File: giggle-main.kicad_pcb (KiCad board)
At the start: 2 copper layers, 97.5 x 97 mm, 27 parts, among them J1 CONN_05X2SHD, J2 CONN_05X2SHD

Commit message: finished main side.
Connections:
- Promicro pad B1: (no net) -> N-col-0
- Promicro pad B2: (no net) -> N-row-1
- Promicro pad B3: (no net) -> N-col-4
- Promicro pad B4: (no net) -> N-row-2
- Promicro pad B5: (no net) -> N-row-3
- Promicro pad B6: (no net) -> N-row-0
- Promicro pad C6: (no net) -> N-col-8
- Promicro pad D0: (no net) -> N-col-11
- Promicro pad D1: (no net) -> N-col-10
- Promicro pad D4: (no net) -> N-col-12
- Promicro pad D7: (no net) -> N-col-7
- Promicro pad E6: (no net) -> N-col-6
- Promicro pad F4: (no net) -> N-col-5
- Promicro pad F5: (no net) -> N-col-3
- Promicro pad F6: (no net) -> N-col-2
- Promicro pad F7: (no net) -> N-col-1
- Promicro pad RX1: (no net) -> N-col-9
- Promicro pad TX0: (no net) -> N-col-13
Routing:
- net N-col-13: track 0.00 -> 100.8 mm
- net N-col-9: track 0.00 -> 90.7 mm
- net N-col-5: track 43.2 -> 131.1 mm
- net N-col-10: track 0.00 -> 83.6 mm
- net N-col-11: track 0.00 -> 79.9 mm
- net N-col-12: track 0.00 -> 78.3 mm
- net N-col-3: track 0.00 -> 69.0 mm
- net N-col-6: track 43.2 -> 110.7 mm
- net N-row-2: track 250.9 -> 316.6 mm
- net N-col-2: track 0.00 -> 65.5 mm
- net N-row-3: track 259.0 -> 323.9 mm
- net N-col-1: track 0.00 -> 61.2 mm
- net N-col-0: track 0.00 -> 58.3 mm
- net N-row-1: track 205.3 -> 254.6 mm
- net N-col-4: track 0.00 -> 46.7 mm
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
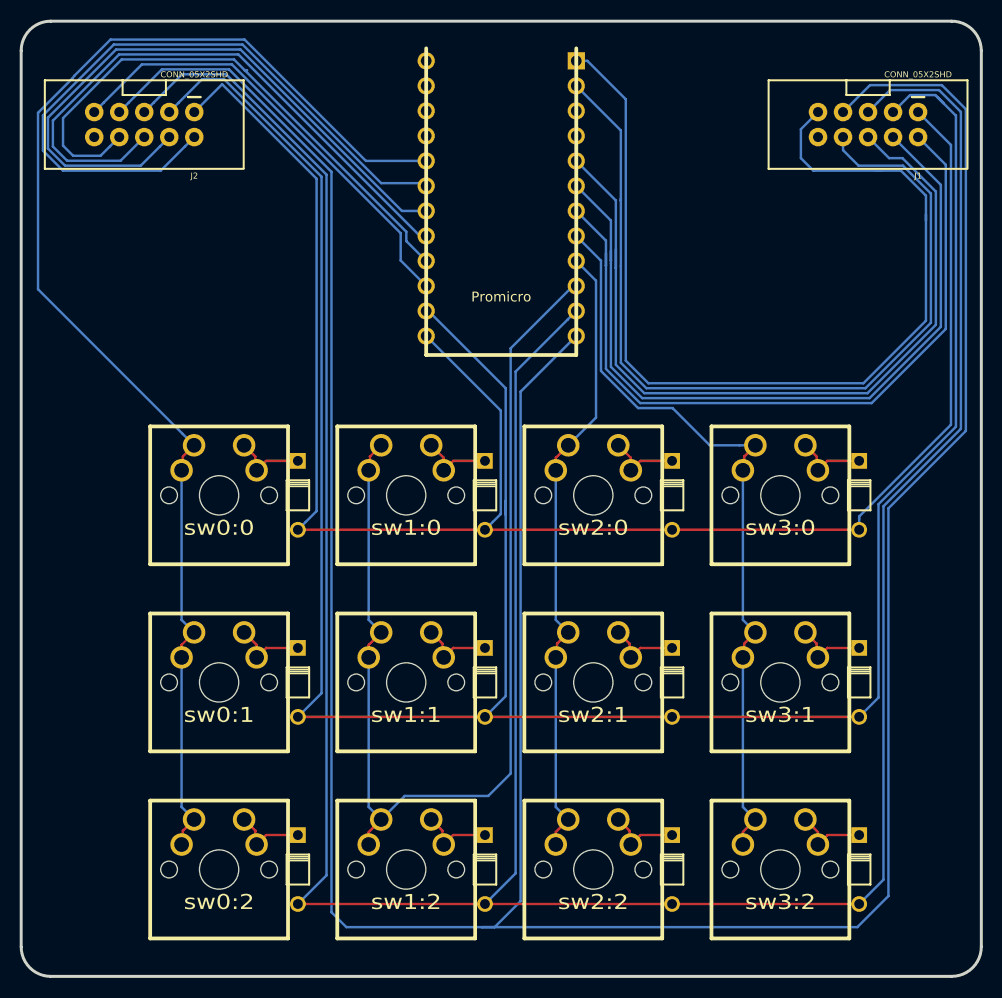
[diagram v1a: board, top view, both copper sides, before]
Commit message: some thing.
1. added another connector on side part.
2. nicer traces.
3. added the giggle text.
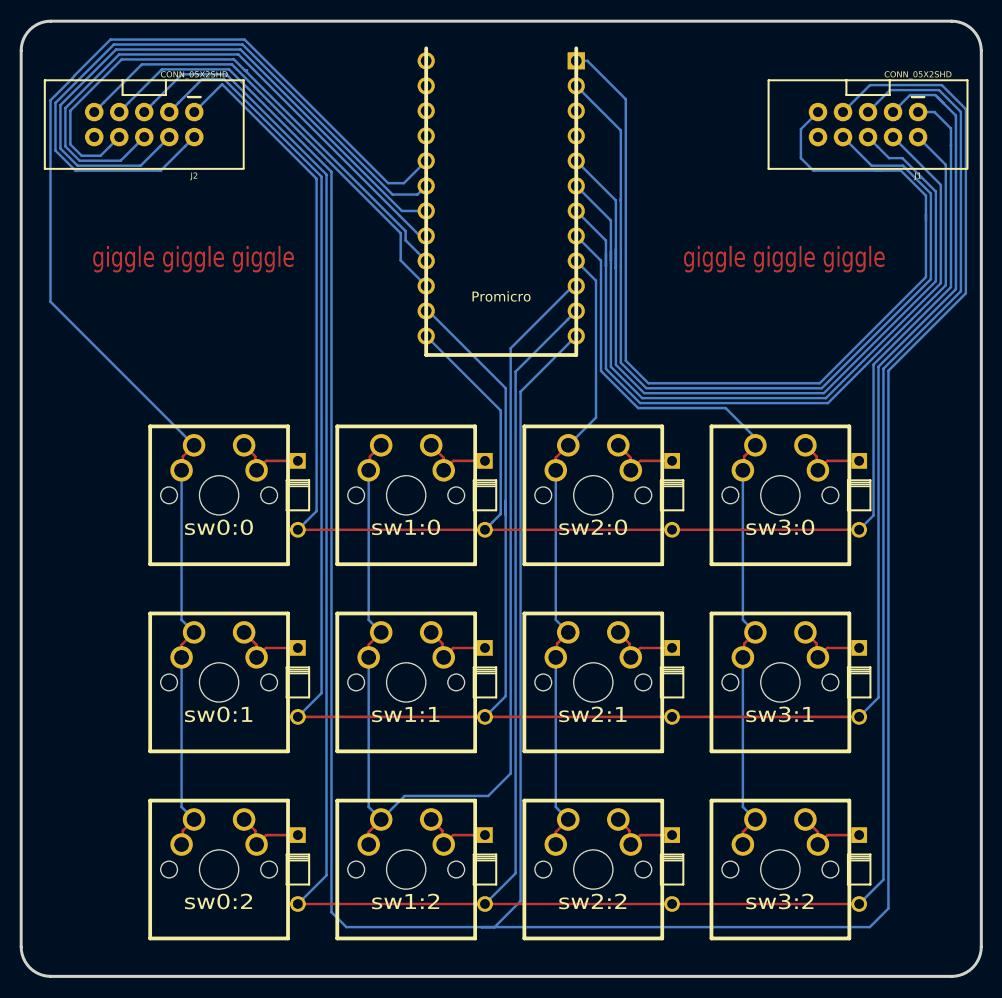
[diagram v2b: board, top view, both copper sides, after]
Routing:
- net N-col-9: track 90.7 -> 87.3 mm
- net N-col-12: track 78.3 -> 75.7 mm
- net N-col-11: track 79.9 -> 77.3 mm
- net N-col-10: track 83.6 -> 81.0 mm
- net N-col-13: track 100.8 -> 98.2 mm
- net N-col-2: track 65.5 -> 63.7 mm
- net N-col-1: track 61.2 -> 59.4 mm
- net N-col-0: track 58.3 -> 57.2 mm
- net N-col-3: track 69.0 -> 68.0 mm
- net N-row-0: track 182.1 -> 183.2 mm
- net N-col-5: track 131.1 -> 132.0 mm
- net N-row-3: track 323.9 -> 324.6 mm
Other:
- board text added: "giggle giggle giggle"

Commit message: 4x4 for main.
because why not?
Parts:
- added d0:3: , DIODE, F.Cu at (55.6, 114.2)
- added d1:3: , DIODE, F.Cu at (74.6, 114.2)
- added d2:3: , DIODE, F.Cu at (93.6, 114.2)
- added d3:3: , DIODE, F.Cu at (112.6, 114.2)
- added sw0:3: , MX_FLIP, F.Cu at (47.6, 114.2)
- added sw1:3: , MX_FLIP, F.Cu at (66.6, 114.2)
- added sw2:3: , MX_FLIP, F.Cu at (85.6, 114.2)
- added sw3:3: , MX_FLIP, F.Cu at (104.6, 114.2)
- moved d0:0 19.0 mm to (55.6, 57.1)
- moved d1:0 19.0 mm to (74.6, 57.1)
- moved d2:0 19.0 mm to (93.6, 57.1)
- moved d3:0 19.0 mm to (112.6, 57.1)
- moved sw0:0 19.0 mm to (47.6, 57.1)
- moved sw1:0 19.0 mm to (66.6, 57.1)
- moved sw2:0 19.0 mm to (85.6, 57.1)
- moved sw3:0 19.0 mm to (104.6, 57.1)
- moved d0:1 19.0 mm to (55.6, 76.2)
- moved d0:2 19.0 mm to (55.6, 95.2)
- moved d1:1 19.0 mm to (74.6, 76.2)
- moved d1:2 19.0 mm to (74.6, 95.2)
- moved d2:1 19.0 mm to (93.6, 76.2)
- moved d2:2 19.0 mm to (93.6, 95.2)
- moved d3:1 19.0 mm to (112.6, 76.2)
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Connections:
- Promicro pad B1: N-col-0 -> N-row-0
- Promicro pad B2: N-row-1 -> N-row-2
- Promicro pad B3: N-col-4 -> N-row-1
- Promicro pad B4: N-row-2 -> N-col-9
- Promicro pad B5: N-row-3 -> N-col-13
- Promicro pad B6: N-row-0 -> N-row-3
- Promicro pad C6: N-col-8 -> N-col-12
- Promicro pad D0: N-col-11 -> N-col-0
- Promicro pad D1: N-col-10 -> N-col-1
- Promicro pad D4: N-col-12 -> N-col-4
- Promicro pad D7: N-col-7 -> N-col-11
- Promicro pad E6: N-col-6 -> N-col-10
- Promicro pad F5: N-col-3 -> N-col-6
- Promicro pad F6: N-col-2 -> N-col-7
- Promicro pad F7: N-col-1 -> N-col-8
- Promicro pad RX1: N-col-9 -> N-col-2
- Promicro pad TX0: N-col-13 -> N-col-3
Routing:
- net N-row-2: track 316.6 -> 190.5 mm
- net N-row-3: track 324.6 -> 210.5 mm
- net N-row-1: track 254.6 -> 170.4 mm
- net N-col-13: track 98.2 -> 19.6 mm
- net N-col-9: track 87.3 -> 30.1 mm
- net N-col-10: track 81.0 -> 33.7 mm
- net N-col-11: track 77.3 -> 39.0 mm
- net N-col-4: track 46.7 -> 84.1 mm
- net N-row-0: track 183.2 -> 150.4 mm
- net N-col-12: track 75.7 -> 44.3 mm
- net N-col-3: track 68.0 -> 47.9 mm
- net N-col-5: track 132.0 -> 113.9 mm
- net N-col-7: track 63.9 -> 80.9 mm
- net N-col-0: track 57.2 -> 71.8 mm
- net N-col-6: track 110.7 -> 97.4 mm
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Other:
- board text added: "giggle giggle giggle giggle giggle giggle giggle giggle giggle giggle giggle giggle"
- board text removed: "giggle giggle giggle"

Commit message: looks better, i guess.
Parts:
- moved Promicro 6.00 mm to (85.0, 38.5)
- turned J1 to 270 degrees
- turned J2 to 270 degrees
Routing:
- net N-row-2: track 190.5 -> 233.1 mm
- net N-row-3: track 210.5 -> 251.1 mm
- net N-row-1: track 170.4 -> 207.2 mm
- net N-row-0: track 150.4 -> 185.6 mm
- net N-col-4: track 84.1 -> 54.0 mm
- net N-col-3: track 47.9 -> 63.6 mm
- net N-col-9: track 30.1 -> 20.9 mm
- net N-col-2: track 53.8 -> 62.0 mm
- net N-col-0: track 71.8 -> 63.7 mm
- net N-col-13: track 19.6 -> 12.1 mm
- net N-col-10: track 33.7 -> 26.4 mm
- net N-col-11: track 39.0 -> 31.9 mm
- net N-col-12: track 44.3 -> 37.3 mm
- net N-col-8: track 79.0 -> 85.0 mm
- net N-col-6: track 97.4 -> 91.4 mm
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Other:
- net class Default added: clearance 0.254, trace_width 0.25, via_dia 0.889, via_drill 0.635

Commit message: forgot the pcb. lmao.
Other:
- net class Default removed

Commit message: yes.
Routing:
- net N-col-5: track 107.9 -> 188.9 mm
- net N-col-6: track 91.4 -> 168.6 mm
- net N-col-7: track 76.5 -> 148.3 mm
- net N-col-8: track 85.0 -> 128.0 mm

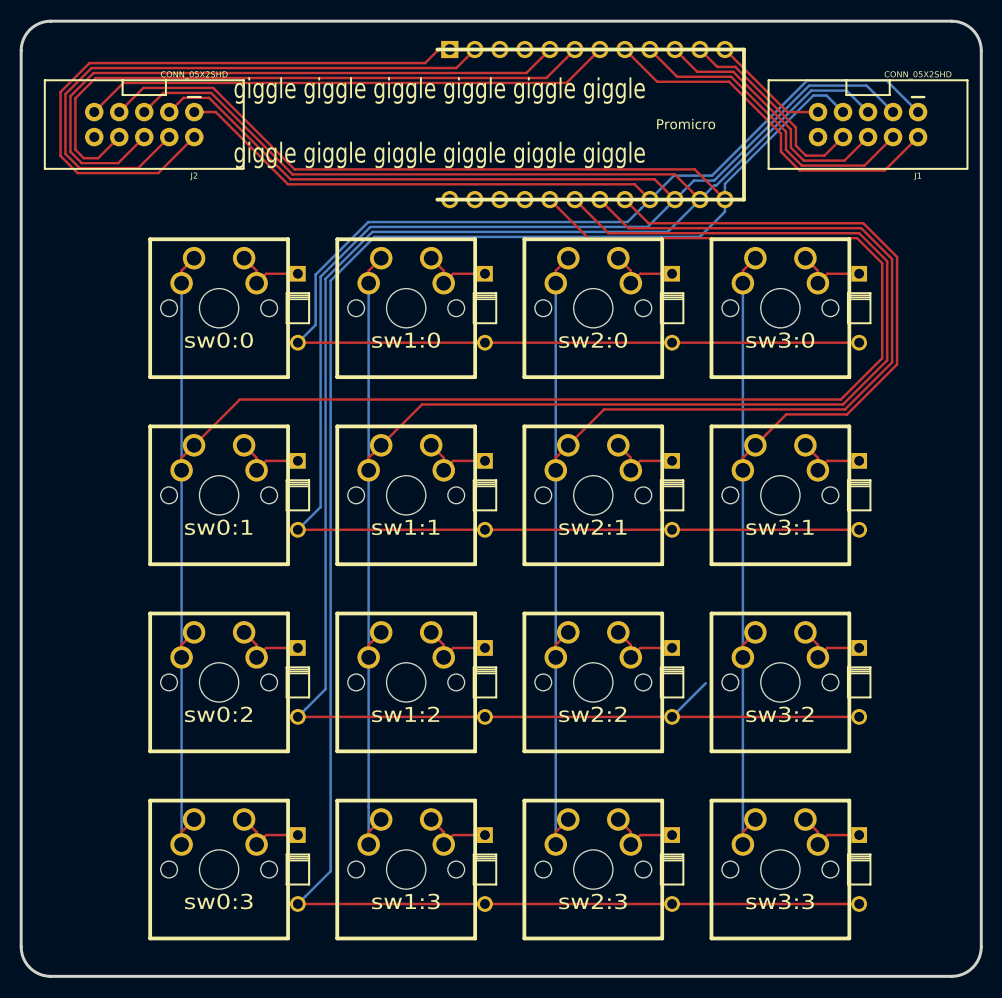
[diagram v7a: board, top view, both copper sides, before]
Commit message: changed switch's footprint and therefore changed the whole traces
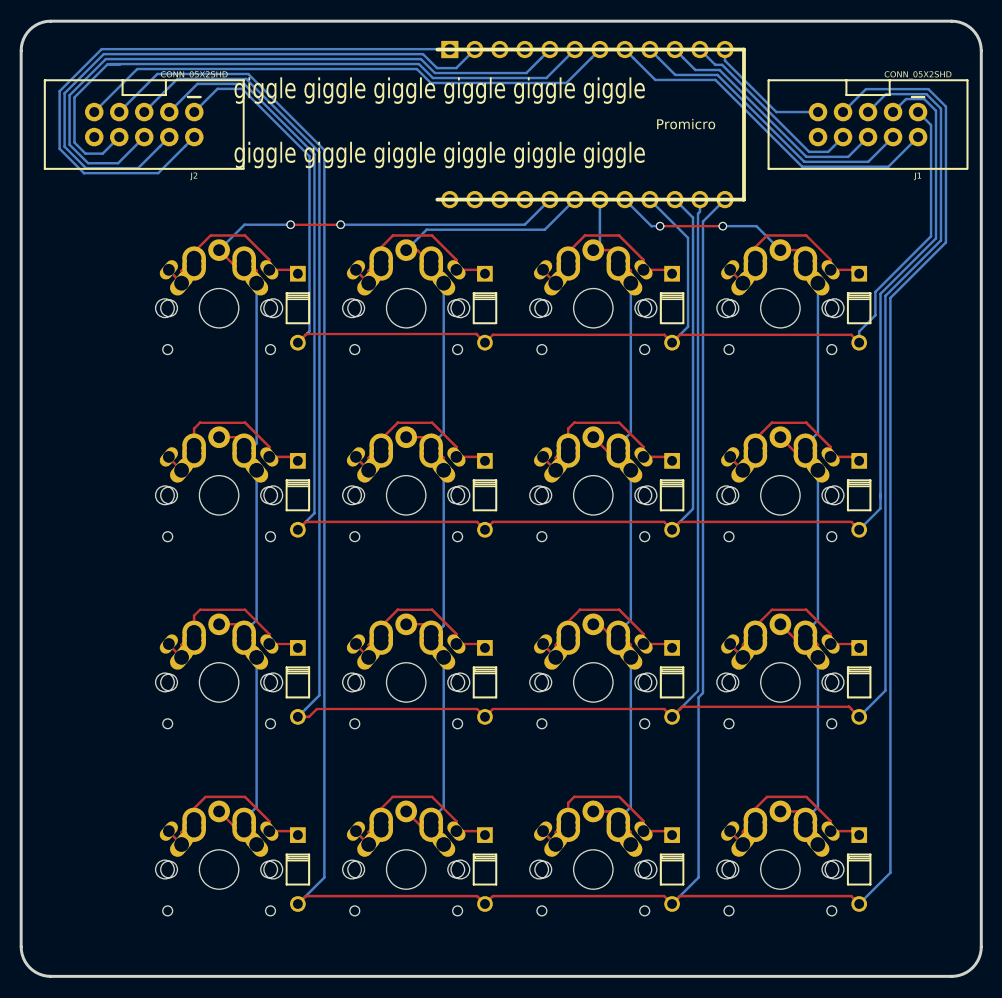
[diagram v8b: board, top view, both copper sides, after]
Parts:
- sw0:0, sw0:1, sw0:2, sw0:3, sw1:0, sw1:1, sw1:2, sw1:3, sw2:0, sw2:1, sw2:2, sw2:3, sw3:0, sw3:1, sw3:2, sw3:3: value (none) -> SW_PUSH; footprint MX_FLIP -> kbd:MX_ALPS_PG1350_noLed
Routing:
- net N-row-3: track 251.1 -> 332.8 mm
- net N-col-5: track 188.9 -> 108.6 mm, vias 0 -> 2
- net N-col-6: track 168.6 -> 92.8 mm
- net N-col-7: track 148.3 -> 79.3 mm
- net N-row-0: track 185.6 -> 137.8 mm
- net N-col-8: track 128.0 -> 91.1 mm, vias 0 -> 2
- net N-row-2: track 233.1 -> 267.4 mm
- net N-diode-6: track 7.65 -> 20.1 mm
- net N-diode-0: track 7.65 -> 20.1 mm
- net N-diode-7: track 7.65 -> 19.9 mm
- net N-diode-15: track 7.65 -> 19.9 mm
- net N-diode-3: track 7.65 -> 19.9 mm
- net N-diode-5: track 7.65 -> 19.6 mm
- net N-diode-14: track 7.65 -> 19.6 mm
- net N-diode-4: track 7.65 -> 19.6 mm
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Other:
- net class Default added: clearance 0.254, trace_width 0.25, via_dia 0.889, via_drill 0.635
